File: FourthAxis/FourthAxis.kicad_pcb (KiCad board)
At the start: 2 copper layers, 135.1 x 114.3 mm, 154 parts, among them J1 36V, J2 DRIVER_CONN, J3 ENC_CONN, J4 HW_CONN, J5 SCREEN_CONN, J6 PROG_HEADER, SW1 NUM_1, SW10 NUM_6, SW11 NUM_9, SW12 PLUS_MINUS, SW13 DELETE, SW14 ENTER, SW15 SET_ZERO, SW16 SET_SPLN, SW17 ANG_ABS, SW18 ROT_CCW, SW19 RET_ZERO, SW2 NUM_4, SW20 NXT_SPLN, SW21 ANG_INC, SW22 ROT_CW, SW23 EXTRA_1, SW24 EXTRA_2, SW25 EXTRA_3, SW26 EXTRA_4, SW27 MODE_SWITCH, SW28 MULT_SWITCH, SW29 BOOT, SW3 NUM_7, SW30 RESET, SW4 DECIMAL, SW5 NUM_2, SW6 NUM_5, SW7 NUM_8, SW8 NUM_0, SW9 NUM_3, U1 ESP32-WROOM-32, U10 SN74LVC1T45DBV, U11 MAX3485, U12 MAX3485, U13 MAX3485, U2 74HC237, U3 SN74LVC1T45DBV, U4 SN74LVC1T45DBV, U5 XL1509-5.0, U6 XL1509-3.3, U7 SN74LVC1T45DBV, U8 SN74LVC1T45DBV, U9 SN74LVC1T45DBV

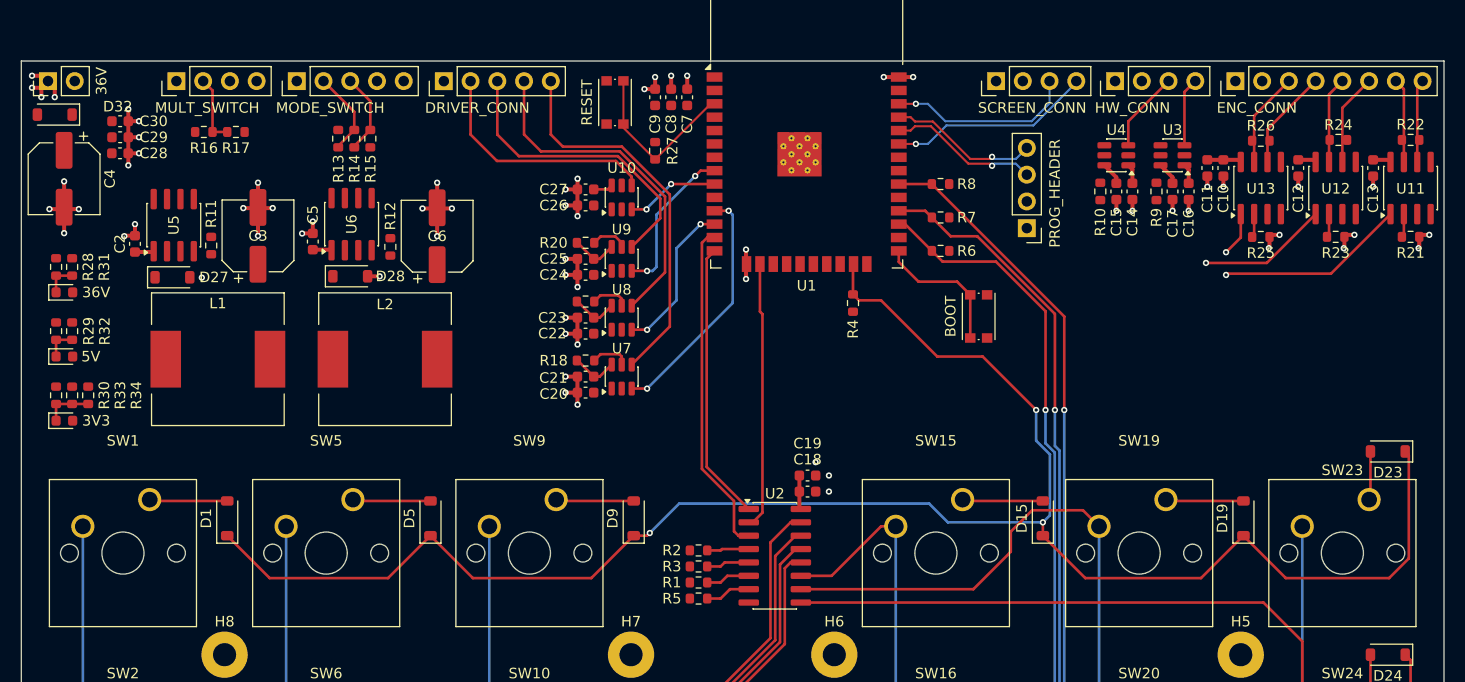
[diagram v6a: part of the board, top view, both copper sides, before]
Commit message: traces almost complete
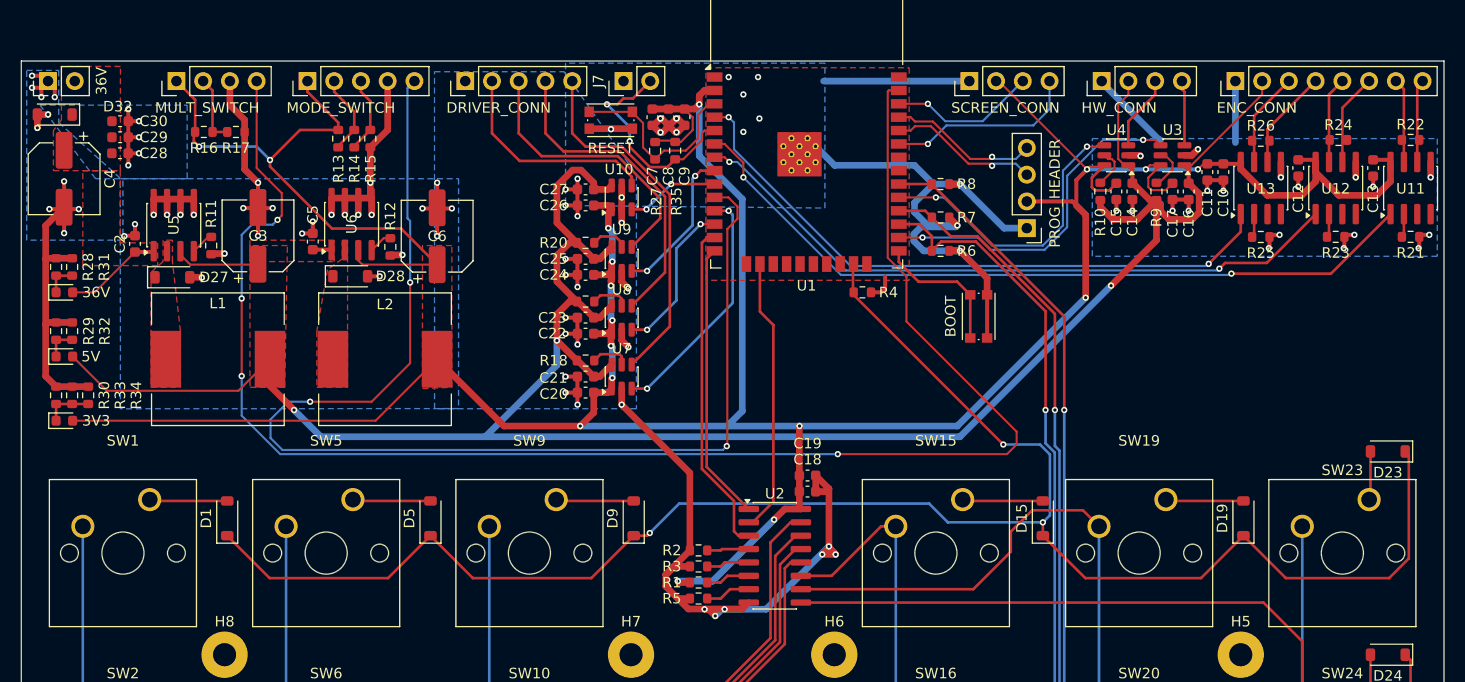
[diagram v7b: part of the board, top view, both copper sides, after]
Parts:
- added J7: ESTOP, Connector_PinHeader_2.54mm:PinHeader_1x02_P2.54mm_Vertical, F.Cu at (99.6, 43.8)
- added R35: 10k, Resistor_SMD:R_0603_1608Metric, F.Cu at (104.5, 50.4)
- moved C7 3.81 mm to (102.4, 47.2), turned to 90 degrees
- moved C9 3.37 mm to (105.4, 47.2), turned to 90 degrees
- moved J5 2.54 mm to (132.5, 43.8)
- moved J2 2.03 mm to (84.6, 43.8)
- moved C8 1.91 mm to (103.9, 47.2), turned to 90 degrees
- moved SW30 1.74 mm to (98.4, 47.5), turned to 0 degrees
- moved R4 1.35 mm to (122.3, 63.9), turned to 0 degrees
- moved J4 1.27 mm to (145.0, 43.8)
- moved SW27 1.02 mm to (69.6, 43.8)
- moved C10 0.38 mm to (156.6, 52.5)
- moved C11 0.38 mm to (155.1, 52.5)
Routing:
- net 3V3: track 14.3 -> 347.1 mm, vias 0 -> 17
- net GND: track 90.2 -> 335.8 mm, vias 65 -> 96
- net 5V: track 20.6 -> 228.1 mm, vias 0 -> 3
- net KNOB_1: track 0.00 -> 150.8 mm, vias 0 -> 4
- net KNOB_2: track 0.00 -> 114.1 mm, vias 0 -> 3
- net ENCOD_Z: track 4.20 -> 60.3 mm, vias 1 -> 2
- net ENCOD_A: track 18.0 -> 72.6 mm, vias 1 -> 2
- net ENCOD_B: track 12.3 -> 63.8 mm, vias 1 -> 2
- net HAND_INT: track 0.00 -> 32.7 mm, vias 0 -> 2
- net HAND_DIR: track 0.00 -> 28.4 mm, vias 0 -> 2
- net ESTOP: track 0.00 -> 20.7 mm, vias 0 -> 2
- net /Power Distribution/36V: track 1.81 -> 9.31 mm
- net Net-(U3-DIR): track 0.00 -> 4.12 mm
- net Net-(U4-DIR): track 0.00 -> 3.79 mm
- net SCREEN_CLK: track 17.8 -> 14.0 mm
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- added copper zone on F.Cu, net /Power Distribution/36V
- added copper zone on F.Cu, net 3V3
- added copper zone on F.Cu, net 5V
- added copper zone on B.Cu, net GND
- added copper zone on F.Cu, net GND
- added copper zone on F.Cu, net Net-(D27-K)
- added copper zone on F.Cu, net Net-(D28-K)

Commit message: done?
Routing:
- net GND: track 335.8 -> 431.9 mm
- net KNOB_2: track 114.1 -> 89.7 mm
- net KNOB_1: track 150.8 -> 129.2 mm, vias 4 -> 3
- net ESTOP: track 20.7 -> 26.1 mm, vias 2 -> 0
- net KEY_1: track 173.2 -> 176.5 mm, vias 3 -> 2
- net 3V3: track 347.1 -> 350.0 mm, vias 17 -> 19
- net Net-(U2-Y5): track 91.1 -> 88.7 mm
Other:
- board text added: "ESTOP"
